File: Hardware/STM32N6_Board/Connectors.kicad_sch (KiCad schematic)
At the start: 0 parts

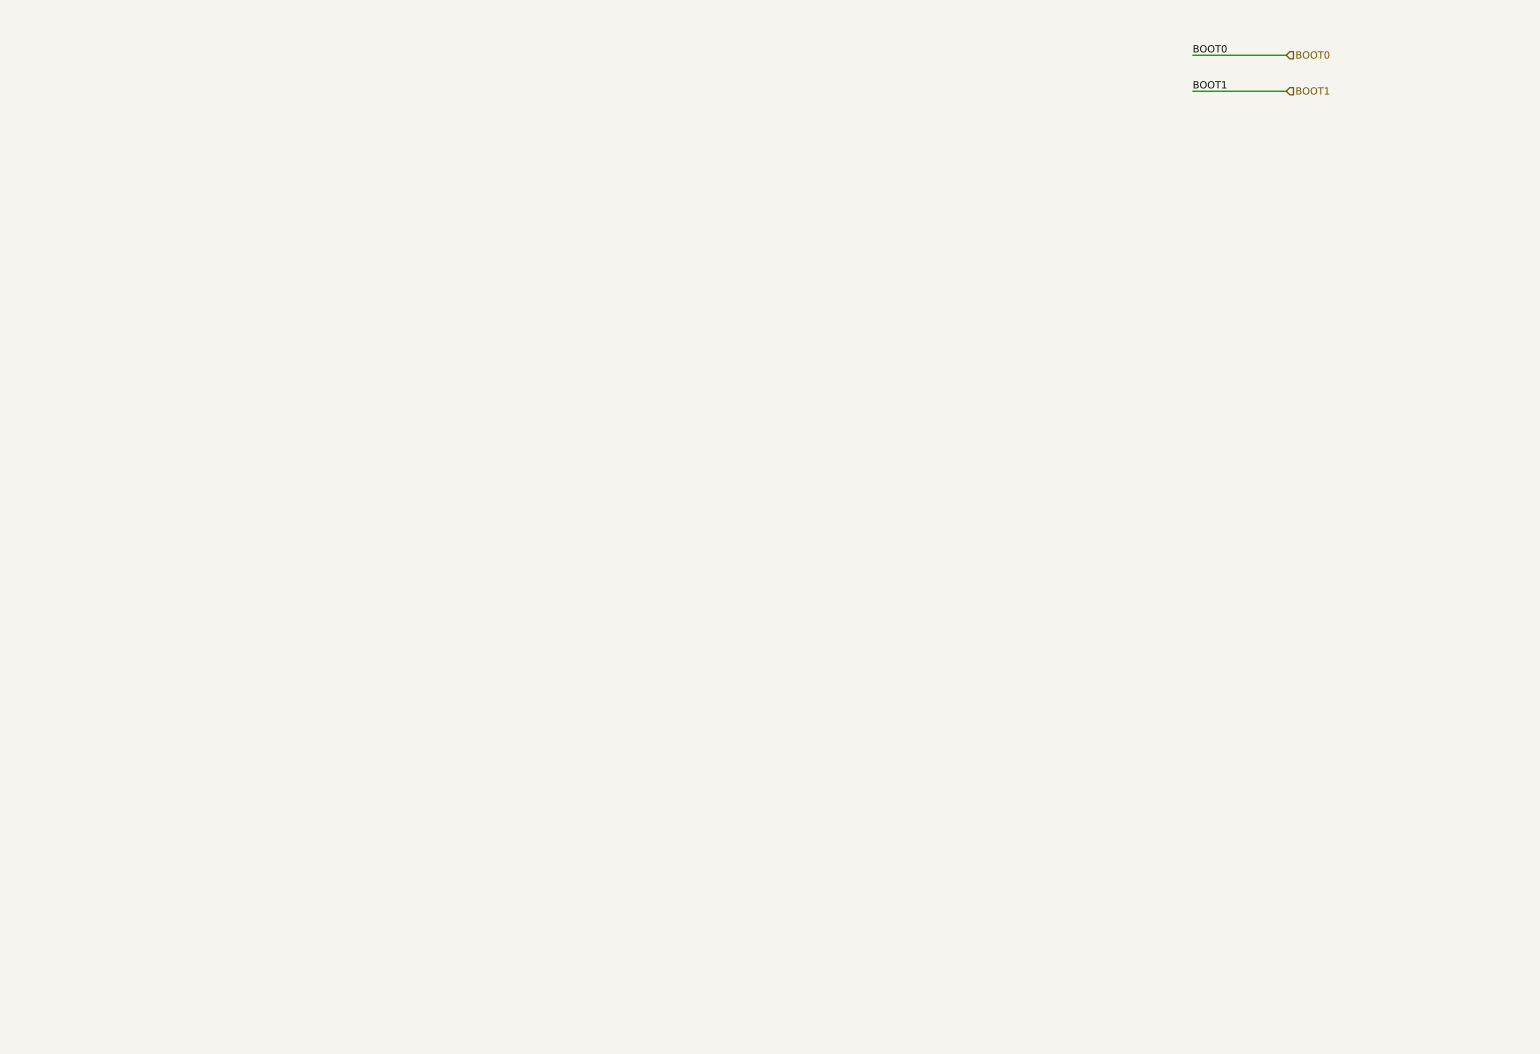
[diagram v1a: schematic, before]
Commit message: Completed the schematic.
- The schematic is complete.
- ERC checker, footprint assignment, and PCB board design left
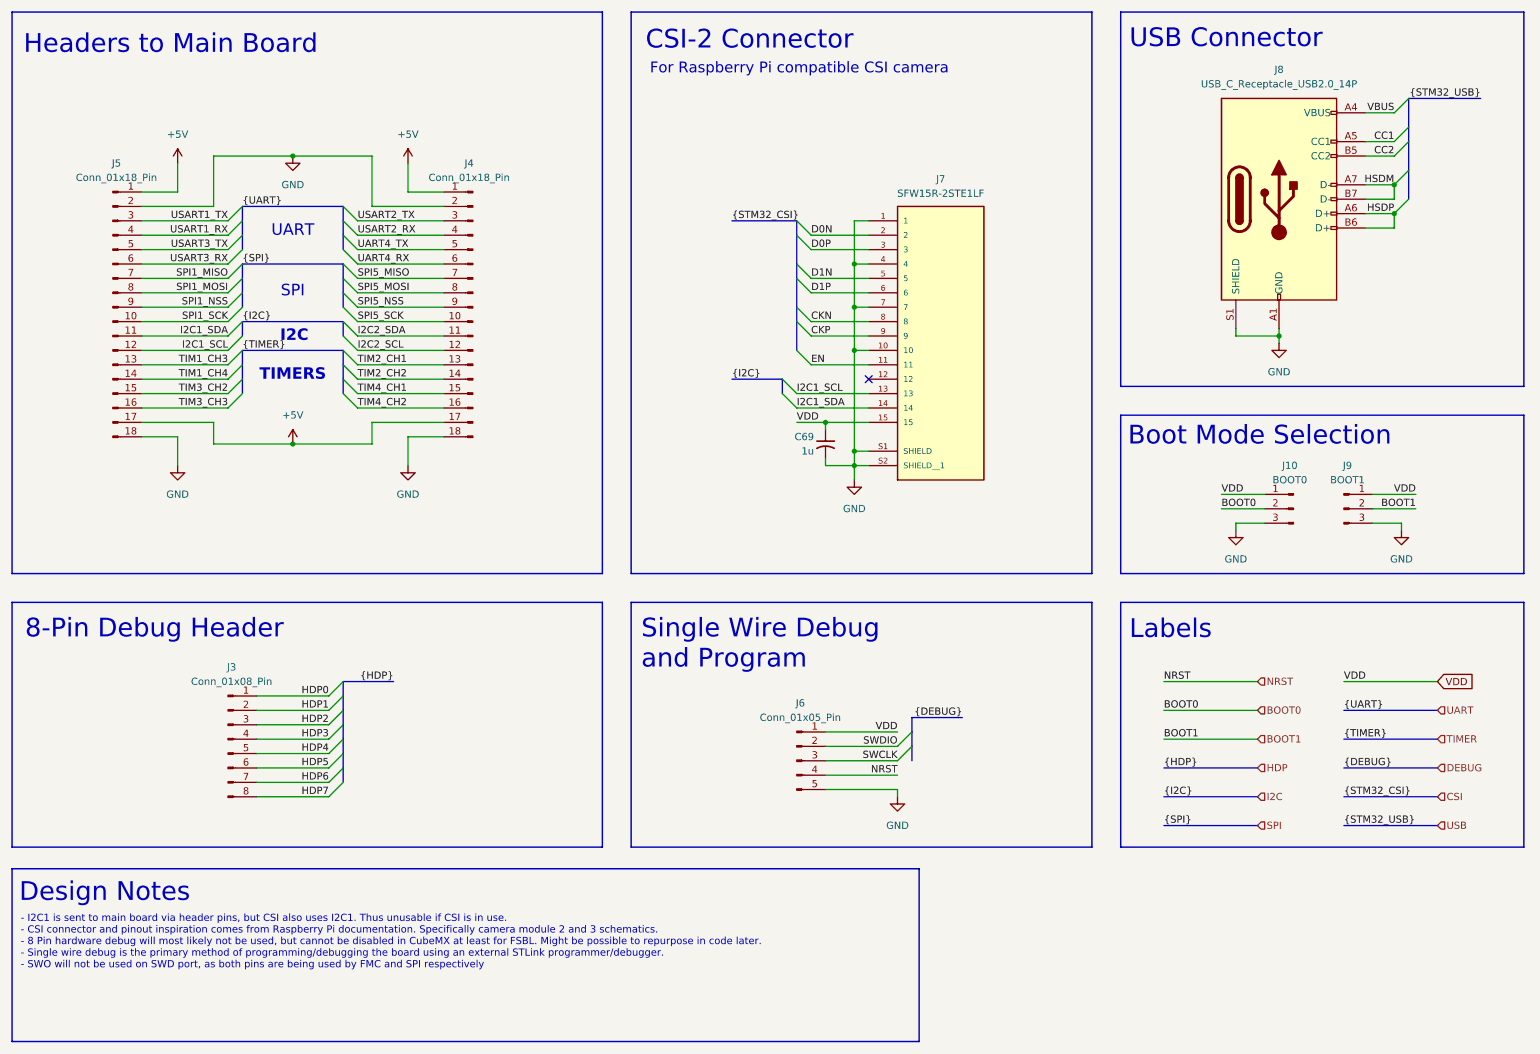
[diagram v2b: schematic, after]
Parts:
- added C69: 1u, symbol Device:C_Small_US
- added J10: BOOT0, symbol Connector:Conn_01x03_Pin
- added J3: Conn_01x08_Pin, symbol Connector:Conn_01x08_Pin
- added J4, J5: Conn_01x18_Pin, symbol Connector:Conn_01x18_Pin
- added J6: Conn_01x05_Pin, symbol Connector:Conn_01x05_Pin
- added J7: SFW15R-2STE1LF, SFW15R-2STE1LF:AMPHENOL_SFW15R-2STE1LF, symbol STM32N6_Symbols:SFW15R-2STE1LF
- added J8: USB_C_Receptacle_USB2.0_14P, symbol Connector:USB_C_Receptacle_USB2.0_14P
- added J9: BOOT1, symbol Connector:Conn_01x03_Pin
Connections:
- net BOOT0: now also J10.2 (Pin_2)
- net BOOT1: now also J9.2 (Pin_2)
- new net +5V: J4.1 (Pin_1), J4.17 (Pin_17), J5.1 (Pin_1), J5.17 (Pin_17)
- new net CC1: J8.A5 (CC1)
- new net CC2: J8.B5 (CC2)
- new net CKN: J7.8
- new net CKP: J7.9
- new net D0N: J7.2
- new net D0P: J7.3
- new net D1N: J7.5
- new net D1P: J7.6
- new net EN: J7.11
- new net GND: C69.2, J10.3 (Pin_3), J4.18 (Pin_18), J4.2 (Pin_2), J5.18 (Pin_18), J5.2 (Pin_2), J6.5 (Pin_5), J7.1, J7.10, J7.4, J7.7, J7.S1 (SHIELD), J7.S2 (SHIELD__1), J8.A1 (GND), J8.A12 (GND), J8.B1 (GND), J8.B12 (GND), J8.S1 (SHIELD), J9.3 (Pin_3)
- new net HDP0: J3.1 (Pin_1)
- new net HDP1: J3.2 (Pin_2)
- new net HDP2: J3.3 (Pin_3)
- new net HDP3: J3.4 (Pin_4)
- new net HDP4: J3.5 (Pin_5)
- new net HDP5: J3.6 (Pin_6)
- new net HDP6: J3.7 (Pin_7)
- new net HDP7: J3.8 (Pin_8)
- new net HSDM: J8.A7 (D-), J8.B7 (D-)
- new net HSDP: J8.A6 (D+), J8.B6 (D+)
- new net I2C1_SCL: J5.12 (Pin_12), J7.13
- new net I2C1_SDA: J5.11 (Pin_11), J7.14
- new net I2C2_SCL: J4.12 (Pin_12)
- new net I2C2_SDA: J4.11 (Pin_11)
- new net NRST: J6.4 (Pin_4)
- new net SPI1_MISO: J5.7 (Pin_7)
- new net SPI1_MOSI: J5.8 (Pin_8)
- new net SPI1_NSS: J5.9 (Pin_9)
- new net SPI1_SCK: J5.10 (Pin_10)
- new net SPI5_MISO: J4.7 (Pin_7)
- new net SPI5_MOSI: J4.8 (Pin_8)
- new net SPI5_NSS: J4.9 (Pin_9)
- new net SPI5_SCK: J4.10 (Pin_10)
- new net SWCLK: J6.3 (Pin_3)
- new net SWDIO: J6.2 (Pin_2)
- new net TIM1_CH3: J5.13 (Pin_13)
- new net TIM1_CH4: J5.14 (Pin_14)
- new net TIM2_CH1: J4.13 (Pin_13)
- new net TIM2_CH2: J4.14 (Pin_14)
- new net TIM3_CH2: J5.15 (Pin_15)
- new net TIM3_CH3: J5.16 (Pin_16)
- new net TIM4_CH1: J4.15 (Pin_15)
- new net TIM4_CH2: J4.16 (Pin_16)
- new net UART4_RX: J4.6 (Pin_6)
- new net UART4_TX: J4.5 (Pin_5)
- new net USART1_RX: J5.4 (Pin_4)
- new net USART1_TX: J5.3 (Pin_3)
- new net USART2_RX: J4.4 (Pin_4)
- new net USART2_TX: J4.3 (Pin_3)
- new net USART3_RX: J5.6 (Pin_6)
- new net USART3_TX: J5.5 (Pin_5)
- new net VBUS: J8.A4 (VBUS), J8.A9 (VBUS), J8.B4 (VBUS), J8.B9 (VBUS)
- new net VDD: C69.1, J10.1 (Pin_1), J6.1 (Pin_1), J7.15, J9.1 (Pin_1)
- no-connect marks 0 -> 1
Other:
- note added: "- I2C1 is sent to main board via header pins, but CSI also uses I2C1. Thus unusable if CSI is in use. - CSI connector and pinout inspiration comes from Raspberry Pi documentation. Specifically camera module 2 and 3 schematics. - 8 Pin hardware debug will most likely not be used, but cannot be disabled in CubeMX at least for FSBL. Might be possible to repurpose in code later. - Single wire debug i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"
- note added: "8-Pin Debug Header"
- note added: "Boot Mode Selection"
- note added: "CSI-2 Connector"
- note added: "Design Notes"
- note added: "For Raspberry Pi compatible CSI camera"
- note added: "Headers to Main Board"
- note added: "I2C"
- note added: "Labels"
- note added: "SPI"
- note added: "Single Wire Debug and Program"
- note added: "TIMERS"
- note added: "UART"
- note added: "USB Connector"
- title: (none) -> SolarVision Mower - STM32N6 Board - Connectors

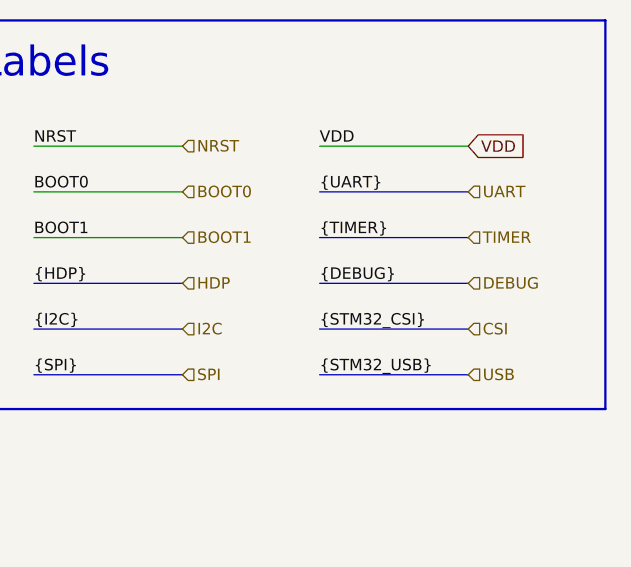
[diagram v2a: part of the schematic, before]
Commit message: Made fixes to remove ERC errors
- 1 remaining error, but > 100 warnings D:
- The remaining error is a bug within KiCAD I believe
- Next is footprint assignment
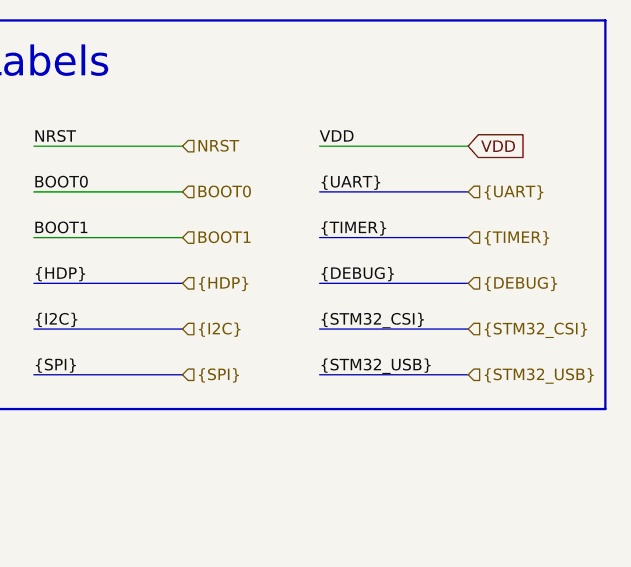
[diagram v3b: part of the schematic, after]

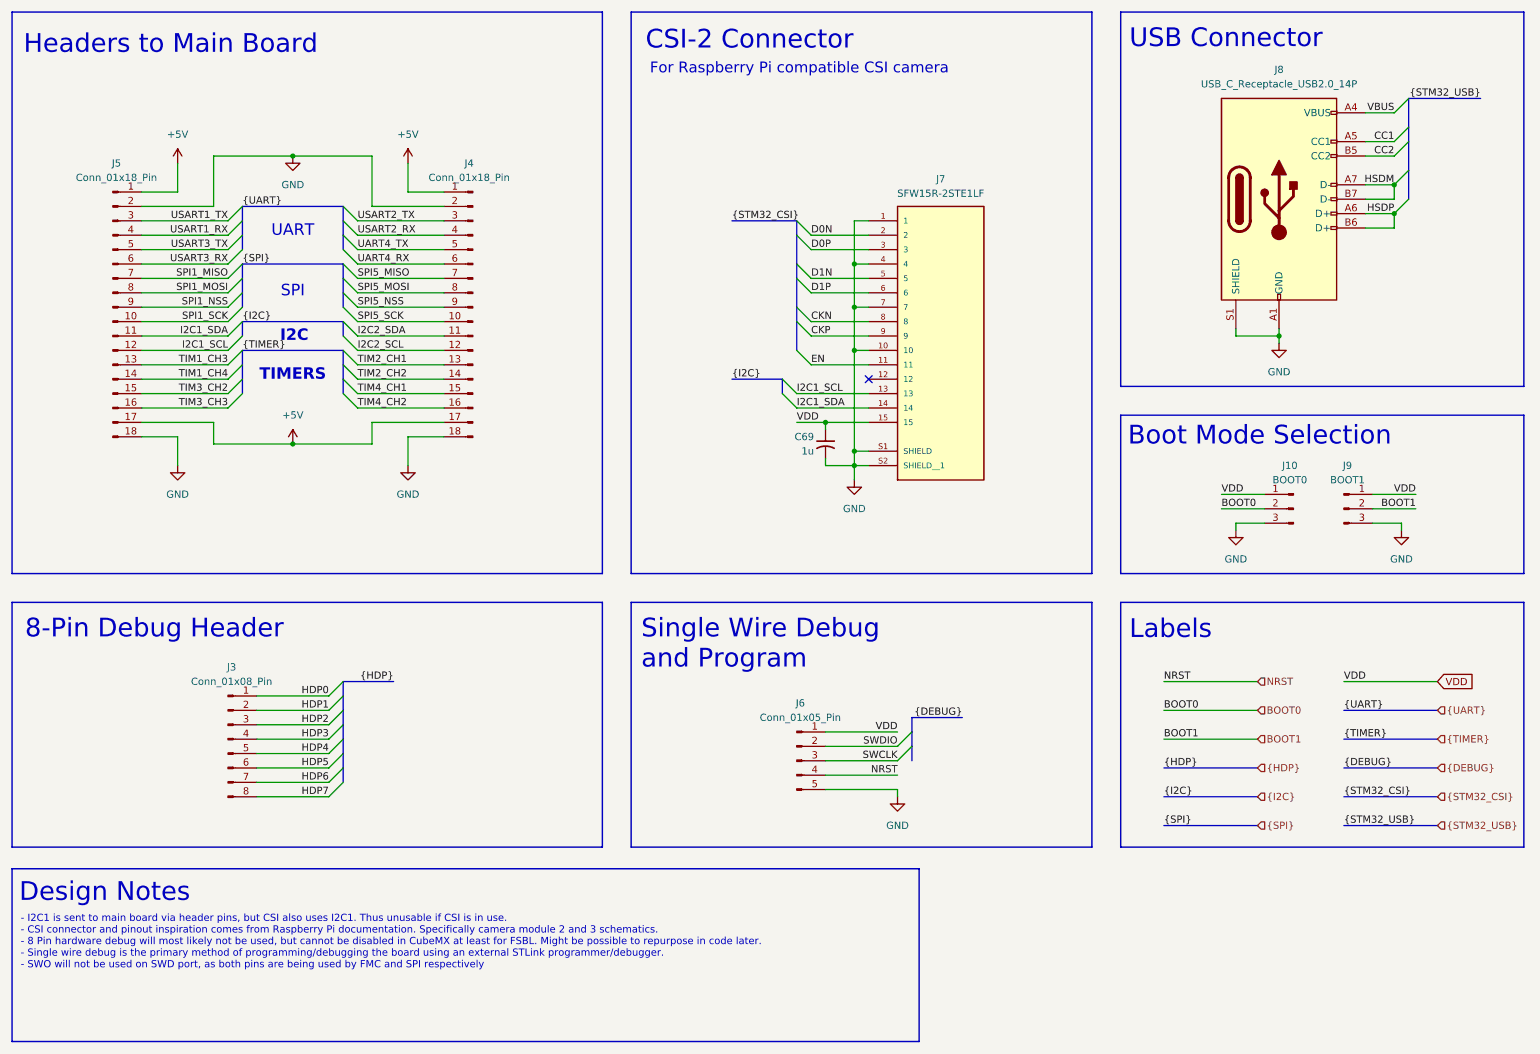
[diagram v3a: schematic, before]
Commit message: Completed schematic layout, ERC check, and footprint assignment
- Completed and checked the schematic layout
- Ran the ERC check; no errors (but lots of (checked) warnings)
- Assigned footprints. Most in std lib, others in footprints.pretty
- Imported the components to the PCB Editor, and fixed errors
- All that's left is PCB layout!
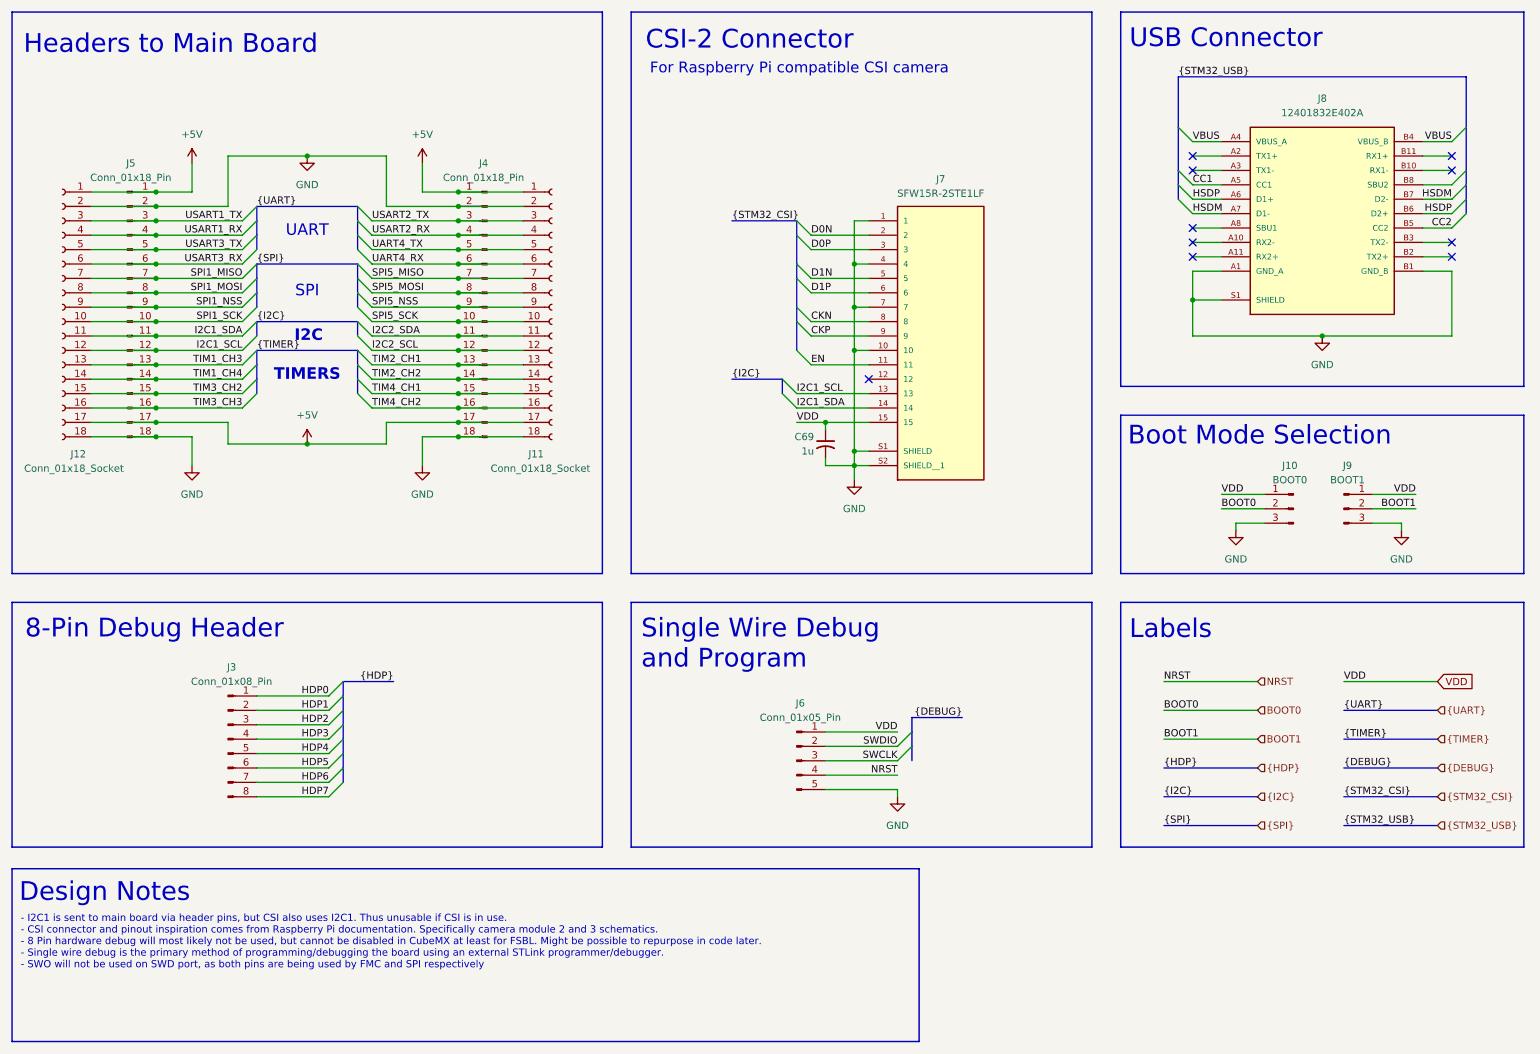
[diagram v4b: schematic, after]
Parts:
- removed J8: USB_C_Receptacle_USB2.0_14P, symbol Connector:USB_C_Receptacle_USB2.0_14P
- added J11, J12: Conn_01x18_Socket, Connector_PinSocket_2.54mm:PinSocket_1x18_P2.54mm_Vertical, symbol Connector:Conn_01x18_Socket
- added J8: 12401832E402A, STM32N6_Footprints:AMPHENOL_12401832E402A, symbol STM32N6_Symbols:12401832E402A
- C69: footprint (none) -> Capacitor_SMD:C_0805_2012Metric_Pad1.18x1.45mm_HandSolder
- J10, J9: footprint (none) -> Connector_PinHeader_2.54mm:PinHeader_1x03_P2.54mm_Vertical
- J3: footprint (none) -> Connector_PinHeader_2.54mm:PinHeader_1x08_P2.54mm_Vertical
- J4, J5: footprint (none) -> Connector_PinHeader_2.54mm:PinHeader_1x18_P2.54mm_Vertical
- J6: footprint (none) -> Connector_PinHeader_2.54mm:PinHeader_1x05_P2.54mm_Vertical
- J7: footprint SFW15R-2STE1LF:AMPHENOL_SFW15R-2STE1LF -> STM32N6_Footprints:AMPHENOL_SFW15R-2STE1LF
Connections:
- net +5V: now also J11.1 (Pin_1), J11.17 (Pin_17), J12.1 (Pin_1), J12.17 (Pin_17)
- net CC1: now also J8.A5 (CC1)
- net CC2: now also J8.B5 (CC2)
- net GND: now also J11.18 (Pin_18), J11.2 (Pin_2), J12.18 (Pin_18), J12.2 (Pin_2), J8.A1 (GND_A), J8.A12 (GND_A), J8.B1 (GND_B), J8.B12 (GND_B), J8.S1 (SHIELD), J8.S2 (SHIELD), J8.S3 (SHIELD), J8.S4 (SHIELD)
- net HSDM: now also J8.A7 (D1-), J8.B7 (D2-)
- net HSDP: now also J8.A6 (D1+), J8.B6 (D2+)
- net I2C1_SCL: now also J12.12 (Pin_12)
- net I2C1_SDA: now also J12.11 (Pin_11)
- net I2C2_SCL: now also J11.12 (Pin_12)
- net I2C2_SDA: now also J11.11 (Pin_11)
- net SPI1_MISO: now also J12.7 (Pin_7)
- net SPI1_MOSI: now also J12.8 (Pin_8)
- net SPI1_NSS: now also J12.9 (Pin_9)
- net SPI1_SCK: now also J12.10 (Pin_10)
- net SPI5_MISO: now also J11.7 (Pin_7)
- net SPI5_MOSI: now also J11.8 (Pin_8)
- net SPI5_NSS: now also J11.9 (Pin_9)
- net SPI5_SCK: now also J11.10 (Pin_10)
- net TIM1_CH3: now also J12.13 (Pin_13)
- net TIM1_CH4: now also J12.14 (Pin_14)
- net TIM2_CH1: now also J11.13 (Pin_13)
- net TIM2_CH2: now also J11.14 (Pin_14)
- net TIM3_CH2: now also J12.15 (Pin_15)
- net TIM3_CH3: now also J12.16 (Pin_16)
- net TIM4_CH1: now also J11.15 (Pin_15)
- net TIM4_CH2: now also J11.16 (Pin_16)
- net UART4_RX: now also J11.6 (Pin_6)
- net UART4_TX: now also J11.5 (Pin_5)
- net USART1_RX: now also J12.4 (Pin_4)
- net USART1_TX: now also J12.3 (Pin_3)
- net USART2_RX: now also J11.4 (Pin_4)
- net USART2_TX: now also J11.3 (Pin_3)
- net USART3_RX: now also J12.6 (Pin_6)
- net USART3_TX: now also J12.5 (Pin_5)
- new net VBUS_A: J8.A4 (VBUS_A), J8.A9 (VBUS_A), J8.B4 (VBUS_B), J8.B9 (VBUS_B)
- no-connect marks 1 -> 10
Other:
- moved on the sheet: J4, J5
